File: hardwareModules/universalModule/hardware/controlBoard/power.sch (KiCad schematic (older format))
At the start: 68 parts

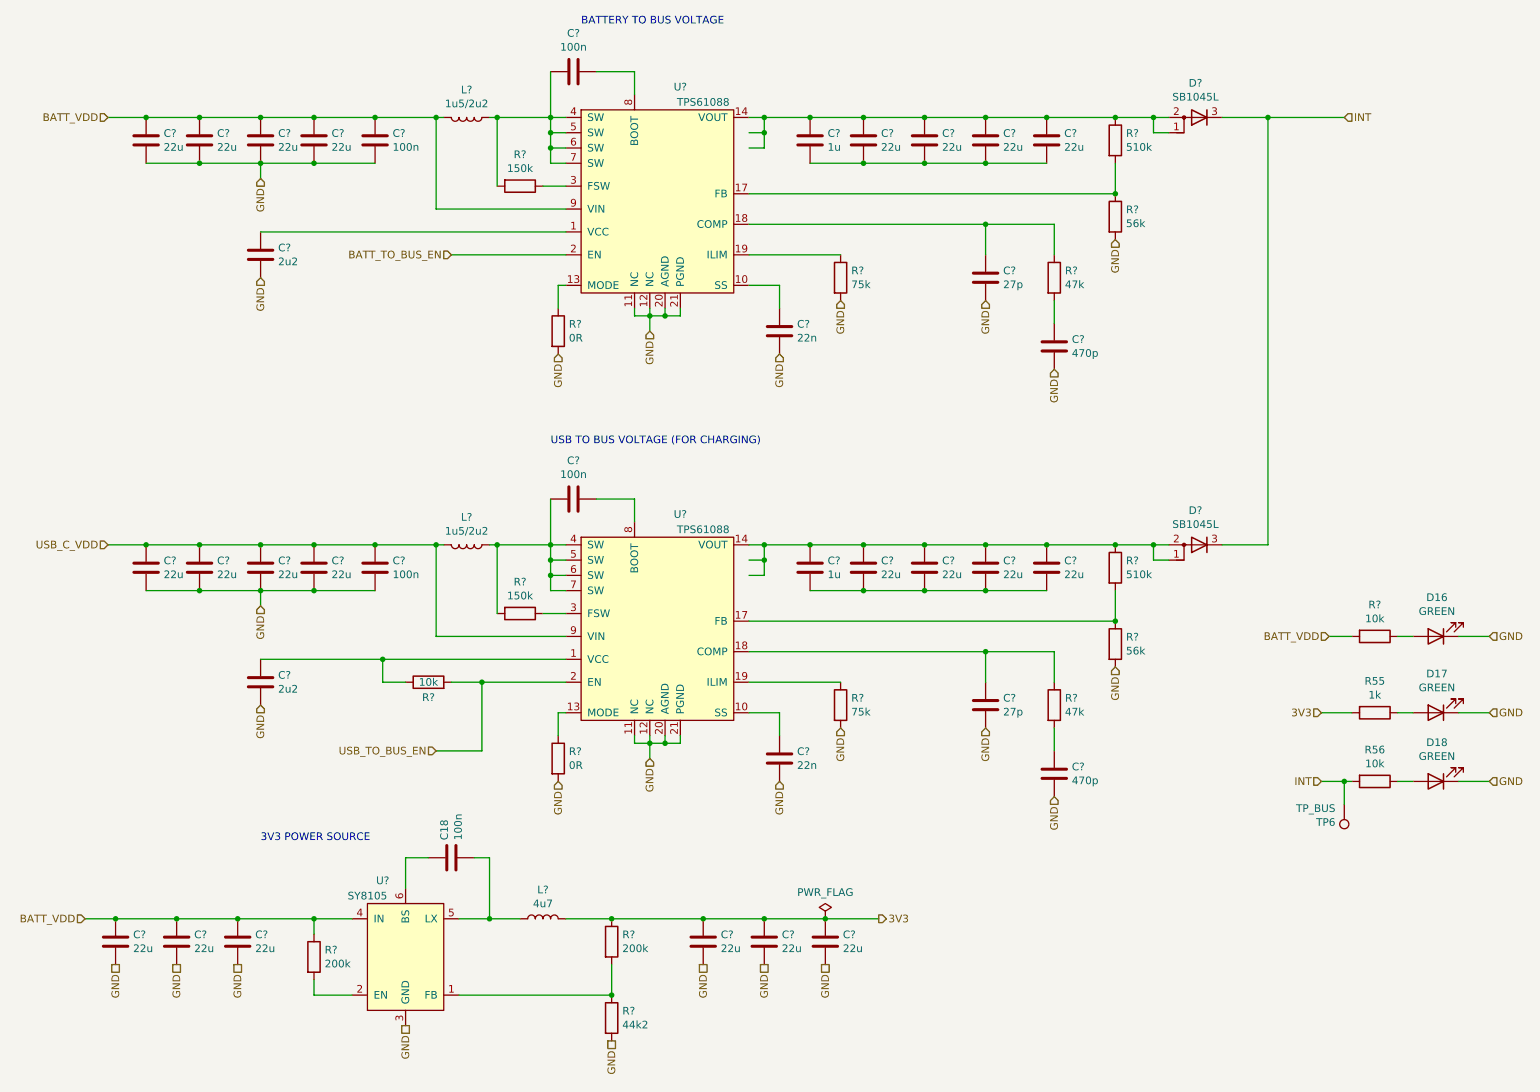
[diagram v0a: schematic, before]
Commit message: universalModule: Draft schematics of the new version of the control board
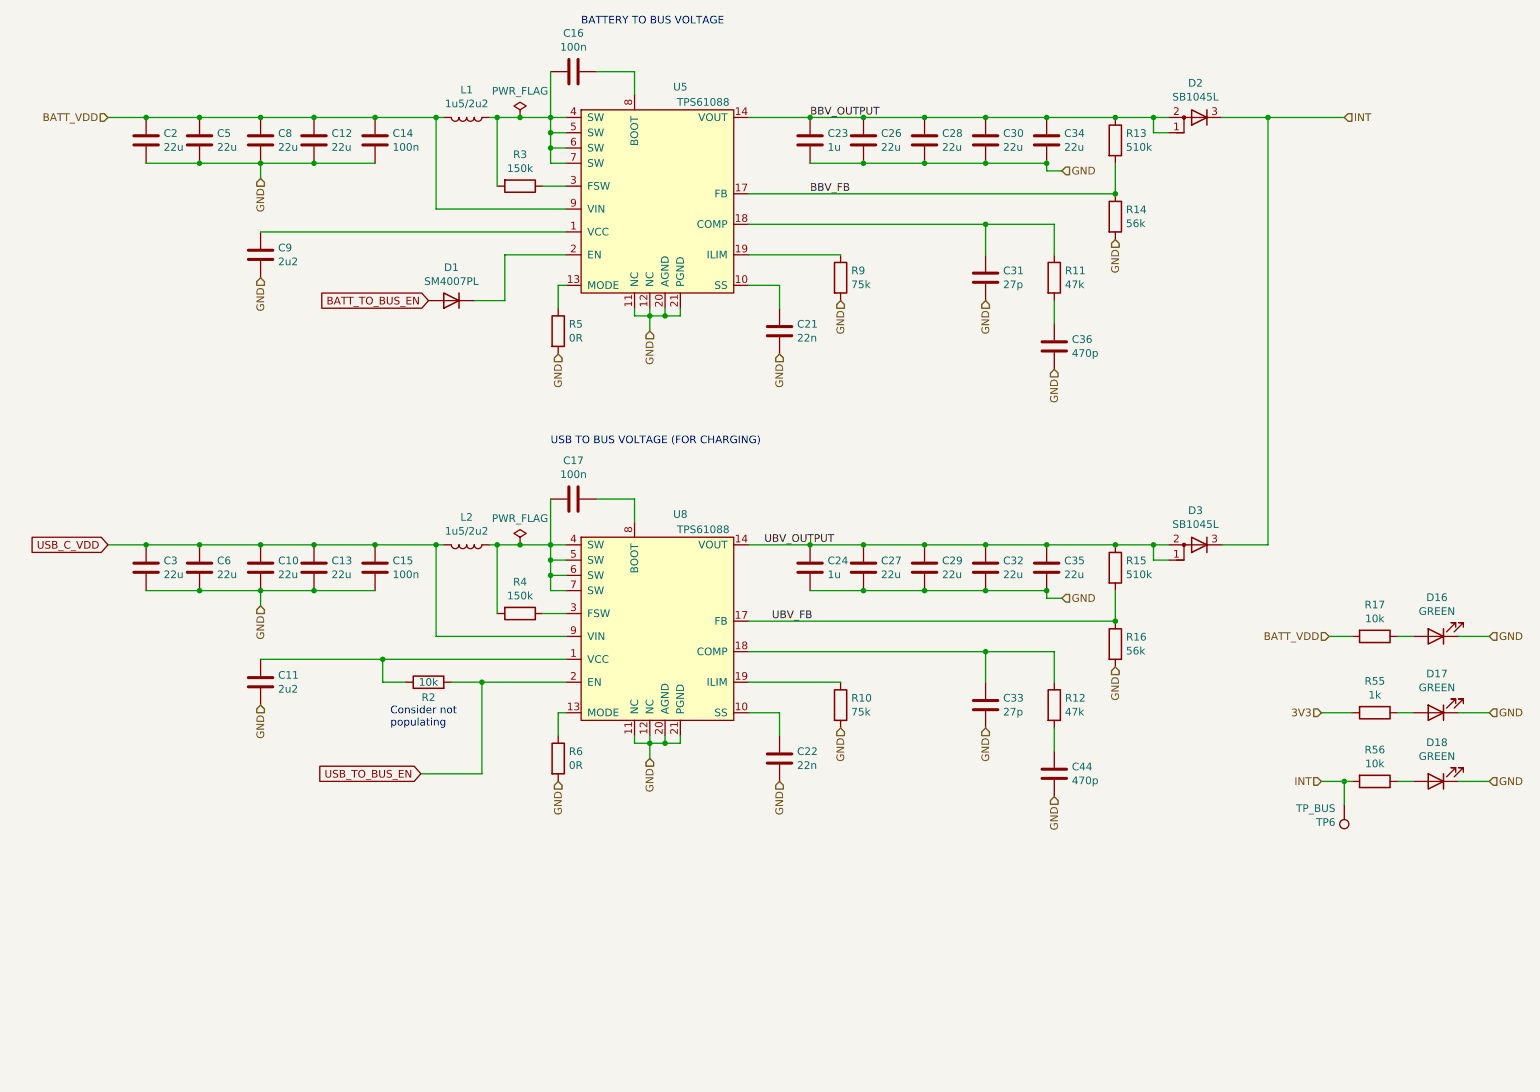
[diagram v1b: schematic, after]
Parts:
- removed C18: 100n, Capacitor_SMD:C_0603_1608Metric, symbol Device:C
- removed C? (x6): 22u, Capacitor_SMD:C_0805_2012Metric, symbol Device:C
- removed L?: 4u7, rofi:SMNR5020, symbol Device:L
- removed R? (x2): 200k, Resistor_SMD:R_0402_1005Metric, symbol Device:R
- removed R?: 44k2, Resistor_SMD:R_0402_1005Metric, symbol Device:R
- removed U?: SY8105, Package_TO_SOT_SMD:TSOT-23-6, symbol rofi:SY8105
- added D1: SM4007PL, Diode_SMD:D_SOD-123F, symbol Device:D
- R10, R9: renamed from R?; footprint (none) -> Resistor_SMD:R_0402_1005Metric
- R2: renamed from R?; footprint (none) -> Resistor_SMD:R_0402_1005Metric; LCSC (none) -> C25744
- gave numbers to parts that had none: 47
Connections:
- net BATT_TO_BUS_EN: now also D1.2 (A); no longer U5.2 (EN)
- net GND: now also C23.2, C24.2, C26.2, C27.2, C28.2, C29.2, C30.2, C32.2, C34.2, C35.2
- net BBV_OUTPUT: now reaches C23.1, C26.1, C28.1, C30.1, C34.1, D2.1 (A), D2.2 (A), R13.1, U5.14 (VOUT), U5.15 (VOUT), U5.16 (VOUT)
- net BBV_FB: now reaches R13.2, R14.1, U5.17 (FB)
- net UBV_OUTPUT: now reaches C24.1, C27.1, C29.1, C32.1, C35.1, D3.1 (A), D3.2 (A), R15.1, U8.14 (VOUT), U8.15 (VOUT), U8.16 (VOUT)
- net UBV_FB: now reaches R15.2, R16.1, U8.17 (FB)
- new net: D1.1 (K), U5.2 (EN)
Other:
- note added: "Consider not\npopulating"
- note removed: "3V3 POWER SOURCE"

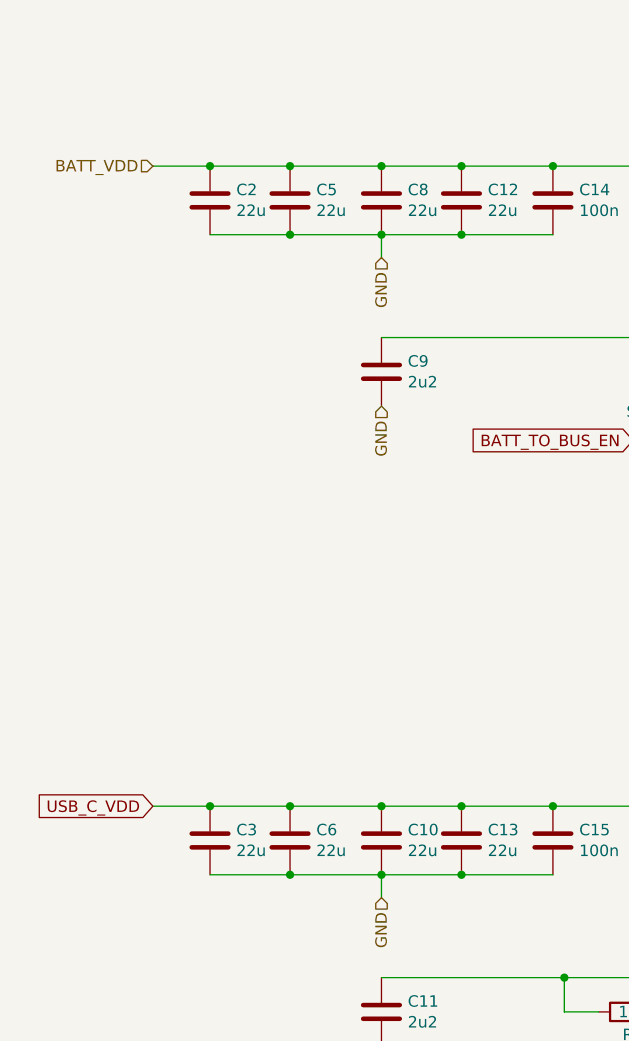
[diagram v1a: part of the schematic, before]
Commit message: universalModule: Prepare electronics v0.2
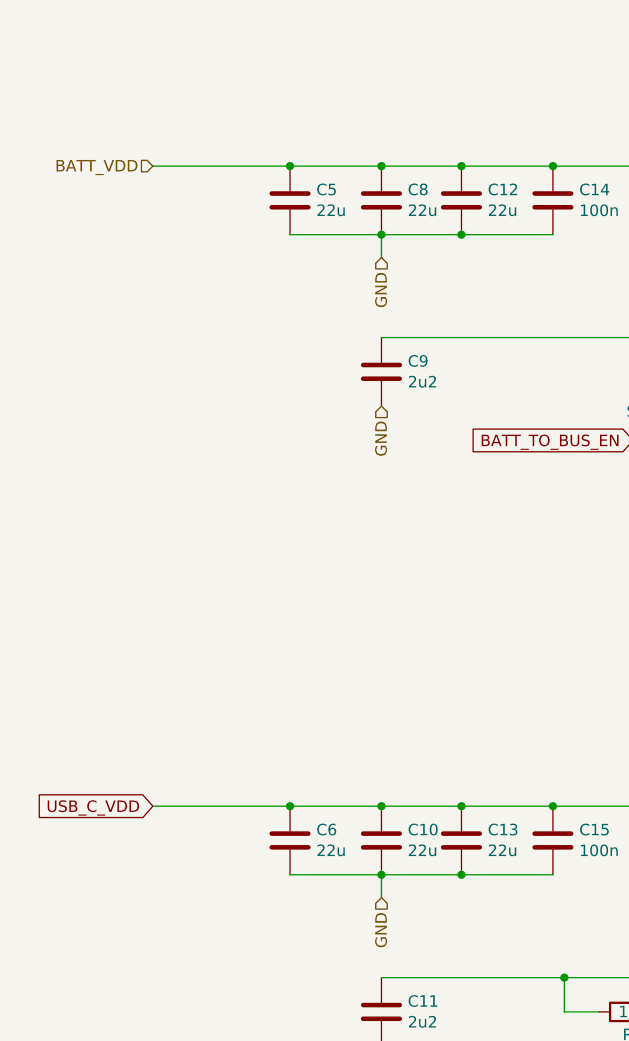
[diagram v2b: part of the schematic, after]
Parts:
- removed C2, C3: 22u, Capacitor_SMD:C_0805_2012Metric, symbol Device:C
- D1, D16, D17, D18: JLCPCB_CORRECTION (none) -> 0;0;180
- D2, D3: JLCPCB_CORRECTION (none) -> 0;0.75;-90
- L1, L2: LCSC (none) -> C149591
- TP6: JLCPCB_IGNORE (none) -> YES
- U5, U8: JLCPCB_CORRECTION (none) -> 0;0;90; LCSC (none) -> C87357
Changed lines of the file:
@@
 $Descr A4 11693 8268
 encoding utf-8
-Sheet 2 5
+Sheet 2 14
 Title ""
 Date ""
@@
 F 3 "~" H 10150 5700 50  0001 C CNN
 F 4 "C72043" H 10150 5700 50  0001 C CNN "LCSC"
+F 5 "0;0;180" H 10150 5700 50  0001 C CNN "JLCPCB_CORRECTION"
 	1    10150 5700
 	-1   0    0    1
@@
 F 3 "~" H 10150 5250 50  0001 C CNN
 F 4 "C72043" H 10150 5250 50  0001 C CNN "LCSC"
+F 5 "0;0;180" H 10150 5250 50  0001 C CNN "JLCPCB_CORRECTION"
 	1    10150 5250
 	-1   0    0    1
@@
 F 3 "~" H 10150 4750 50  0001 C CNN
 F 4 "C72043" H 10150 4750 50  0001 C CNN "LCSC"
+F 5 "0;0;180" H 10150 4750 50  0001 C CNN "JLCPCB_CORRECTION"
 	1    10150 4750
 	-1   0    0    1
@@
 F 2 "TestPoint:TestPoint_Pad_D2.0mm" H 9750 5850 50  0001 C CNN
 F 3 "~" H 9750 5850 50  0001 C CNN
+F 4 "YES" H 9550 5850 50  0001 C CNN "JLCPCB_IGNORE"
 	1    9550 5850
 	-1   0    0    1
@@
 F 3 "~" H 3800 1350 50  0001 C CNN
 F 4 "MGV10043R3M-10" V 3800 1350 50  0001 C CNN "MFR"
+F 5 "C149591" H 3800 1350 50  0001 C CNN "LCSC"
 	1    3800 1350
 	0    1    1    0
@@
 F 3 "~" H 8600 1350 50  0001 C CNN
 F 4 "C113945" H 8600 1350 50  0001 C CNN "LCSC"
+F 5 "0;0.75;-90" H 8600 1350 50  0001 C CNN "JLCPCB_CORRECTION"
 	1    8600 1350
 	-1   0    0    1
@@
 Wire Wire Line
 	2450 1650 2800 1650
-Connection ~ 2050 1650
 Wire Wire Line
 	2050 1650 2450 1650
-Wire Wire Line
-	1700 1650 2050 1650
 Connection ~ 2050 1350
-Wire Wire Line
-	2050 1350 1700 1350
 Connection ~ 2450 1350
 Wire Wire Line
@@
 Wire Wire Line
 	2800 1350 2450 1350
-$Comp
-L Device:C C2
-U 1 1 5FF04ADC
-P 1700 1500
-F 0 "C2" H 1815 1546 50  0000 L CNN
-F 1 "22u" H 1815 1455 50  0000 L CNN
-F 2 "Capacitor_SMD:C_0805_2012Metric" H 1738 1350 50  0001 C CNN
-F 3 "~" H 1700 1500 50  0001 C CNN
-F 4 "C45783" H 1700 1500 50  0001 C CNN "LCSC"
-	1    1700 1500
-	1    0    0    -1
-$EndComp
 $Comp
 L Device:C C5
@@
 F 2 "rofi:VFQFN-20-4.5mmx3.5mm" H 4850 1000 50  0001 C CNN
 F 3 "" H 4850 1000 50  0001 C CNN
+F 4 "C87357" H 5050 1900 50  0001 C CNN "LCSC"
+F 5 "0;0;90" H 5050 1900 50  0001 C CNN "JLCPCB_CORRECTION"
 	1    5050 1900
 	1    0    0    -1
@@
 F 3 "~" H 3800 4150 50  0001 C CNN
 F 4 "MGV10043R3M-10" V 3800 4150 50  0001 C CNN "MFR"
+F 5 "C149591" H 3800 4150 50  0001 C CNN "LCSC"
 	1    3800 4150
 	0    1    1    0
@@
 F 3 "~" H 8600 4150 50  0001 C CNN
 F 4 "C113945" H 8600 4150 50  0001 C CNN "LCSC"
+F 5 "0;0.75;-90" H 8600 4150 50  0001 C CNN "JLCPCB_CORRECTION"
 	1    8600 4150
 	-1   0    0    1
@@
 Wire Wire Line
 	2450 4450 2800 4450
-Connection ~ 2050 4450
-Wire Wire Line
-	2050 4450 2450 4450
-Wire Wire Line
-	1700 4450 2050 4450
-Connection ~ 2050 4150
-Wire Wire Line
-	2050 4150 1700 4150
 Connection ~ 2450 4150
-Wire Wire Line
-	2450 4150 2050 4150
 Connection ~ 2800 4150
 Wire Wire Line
 	2800 4150 2450 4150
-$Comp
-L Device:C C3
-U 1 1 601D2917
-P 1700 4300
-F 0 "C3" H 1815 4346 50  0000 L CNN
-F 1 "22u" H 1815 4255 50  0000 L CNN
-F 2 "Capacitor_SMD:C_0805_2012Metric" H 1738 4150 50  0001 C CNN
-F 3 "~" H 1700 4300 50  0001 C CNN
-F 4 "C45783" H 1700 4300 50  0001 C CNN "LCSC"
-	1    1700 4300
-	1    0    0    -1
-$EndComp
-$Comp
-L Device:C C6
-U 1 1 601D2922
-P 2050 4300
-F 0 "C6" H 2165 4346 50  0000 L CNN
-F 1 "22u" H 2165 4255 50  0000 L CNN
-F 2 "Capacitor_SMD:C_0805_2012Metric" H 2088 4150 50  0001 C CNN
-F 3 "~" H 2050 4300 50  0001 C CNN
-F 4 "C45783" H 2050 4300 50  0001 C CNN "LCSC"
-	1    2050 4300
-	1    0    0    -1
-$EndComp
 $Comp
 L Device:C C10
@@
 F 2 "rofi:VFQFN-20-4.5mmx3.5mm" H 4850 3800 50  0001 C CNN
 F 3 "" H 4850 3800 50  0001 C CNN
+F 4 "C87357" H 5050 4700 50  0001 C CNN "LCSC"
+F 5 "0;0;90" H 5050 4700 50  0001 C CNN "JLCPCB_CORRECTION"
 	1    5050 4700
 	1    0    0    -1
 $EndComp
-Wire Wire Line
-	1450 1350 1700 1350
-Connection ~ 1700 1350
-Wire Wire Line
-	1450 4150 1700 4150
-Connection ~ 1700 4150
 Wire Wire Line
 	9050 4150 9050 1350
@@
 F 3 "~" H 3700 2550 50  0001 C CNN
 F 4 "C95872" H 3700 2550 50  0001 C CNN "LCSC"
+F 5 "0;0;180" H 3700 2550 50  0001 C CNN "JLCPCB_CORRECTION"
 	1    3700 2550
 	-1   0    0    1
@@
 Wire Wire Line
 	4150 4150 4350 4150
+Wire Wire Line
+	2050 4450 2450 4450
+Wire Wire Line
+	2450 4150 2050 4150
+Connection ~ 2050 4150
+$Comp
+L Device:C C6
+U 1 1 601D2922
+P 2050 4300
+F 0 "C6" H 2165 4346 50  0000 L CNN
+F 1 "22u" H 2165 4255 50  0000 L CNN
+F 2 "Capacitor_SMD:C_0805_2012Metric" H 2088 4150 50  0001 C CNN
+F 3 "~" H 2050 4300 50  0001 C CNN
+F 4 "C45783" H 2050 4300 50  0001 C CNN "LCSC"
+	1    2050 4300
+	1    0    0    -1
+$EndComp
+Wire Wire Line
+	1450 4150 2050 4150
+Wire Wire Line
+	1450 1350 2050 1350
 $EndSCHEMATC

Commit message: universalModule: Add final pre-production tweaks
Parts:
- D1, D16, D17, D18: JLCPCB_CORRECTION 0;0;180 -> (none)
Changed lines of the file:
@@
 F 3 "~" H 10150 5700 50  0001 C CNN
 F 4 "C72043" H 10150 5700 50  0001 C CNN "LCSC"
-F 5 "0;0;180" H 10150 5700 50  0001 C CNN "JLCPCB_CORRECTION"
 	1    10150 5700
 	-1   0    0    1
@@
 F 3 "~" H 10150 5250 50  0001 C CNN
 F 4 "C72043" H 10150 5250 50  0001 C CNN "LCSC"
-F 5 "0;0;180" H 10150 5250 50  0001 C CNN "JLCPCB_CORRECTION"
 	1    10150 5250
 	-1   0    0    1
@@
 F 3 "~" H 10150 4750 50  0001 C CNN
 F 4 "C72043" H 10150 4750 50  0001 C CNN "LCSC"
-F 5 "0;0;180" H 10150 4750 50  0001 C CNN "JLCPCB_CORRECTION"
 	1    10150 4750
 	-1   0    0    1
@@
 F 3 "~" H 3700 2550 50  0001 C CNN
 F 4 "C95872" H 3700 2550 50  0001 C CNN "LCSC"
-F 5 "0;0;180" H 3700 2550 50  0001 C CNN "JLCPCB_CORRECTION"
 	1    3700 2550
 	-1   0    0    1
